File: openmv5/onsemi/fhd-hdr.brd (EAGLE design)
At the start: 35.6 x 16.5 mm, 75 parts, among them IC1 AR0231AT7C00XUEA0-DRBR-E, IC2 TLV62568PDDCR, IC3 MIC5365-2.8YC5-TR, J1 DF12-36-DP, Q1 PMXB120EPEZ

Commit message: Finish out new onsemi cameras
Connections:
- net SPI_MISO: now also IC1.K11
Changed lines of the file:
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@@
 <signal name="SPI_MISO" class="4">
 <contactref element="J1" pad="15"/>
+<contactref element="IC1" pad="K11"/>
+<wire x1="21.18" y1="4.89" x2="18.53" y2="10.8999" width="0" layer="19" extent="1-16"/>
 </signal>
 <signal name="SPI_MOSI" class="4">

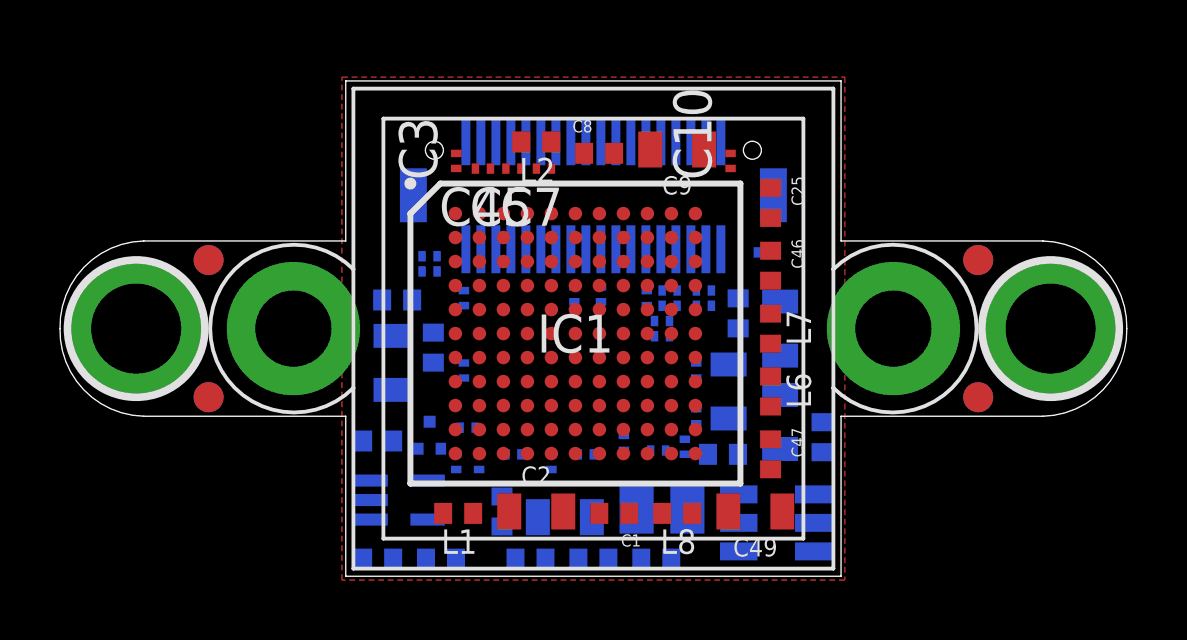
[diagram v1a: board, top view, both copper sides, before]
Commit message: Update camera modules to use different non-flippable pmosfet
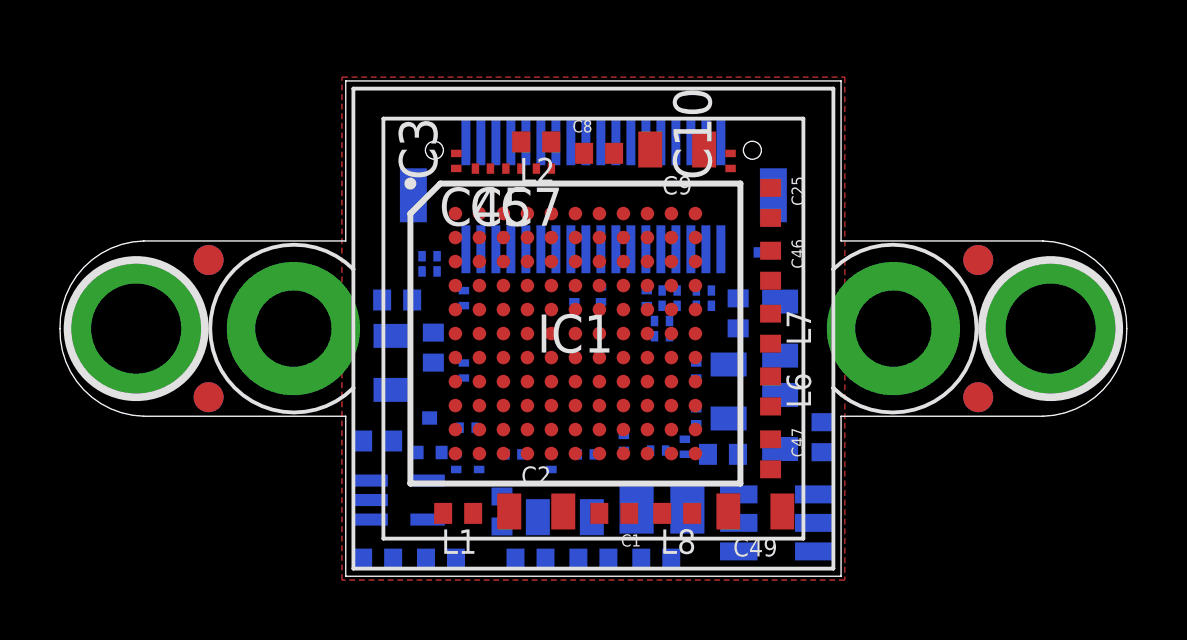
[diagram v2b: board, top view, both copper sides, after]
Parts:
- Q1: value PMXB120EPEZ -> SSM3J15FV,L3F; device PMXB120EPEZ:PMXB120EPEZ -> SSM3J15FV_L3F:SSM3J15FVL3F
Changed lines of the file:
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@@
 <attribute name="VALUE" x="15.875" y="1.27" size="0.6096" layer="27" font="vector" ratio="20" align="top-center"/>
 </element>
-<element name="Q1" library="PMXB120EPEZ" package="PMXB120EPEZ" value="PMXB120EPEZ" x="12.319" y="4.699" smashed="yes" rot="MR0">
-<attribute name="DESCRIPTION" value="MOSFET 30 V, P-channel Trench MOSFET" x="15.367" y="4.699" size="1.778" layer="28" rot="MR0" display="off"/>
-<attribute name="HEIGHT" value="0.4mm" x="15.367" y="4.699" size="1.778" layer="28" rot="MR0" display="off"/>
-<attribute name="MANUFACTURER_NAME" value="Nexperia" x="15.367" y="4.699" size="1.778" layer="28" rot="MR0" display="off"/>
-<attribute name="MANUFACTURER_PART_NUMBER" value="PMXB120EPEZ" x="15.367" y="4.699" size="1.778" layer="28" rot="MR0" display="off"/>
-<attribute name="MOUSER_PART_NUMBER" value="771-PMXB120EPEZ" x="15.367" y="4.699" size="1.778" layer="28" rot="MR0" display="off"/>
-<attribute name="MOUSER_PRICE-STOCK" value="https://www.mouser.co.uk/ProductDetail/Nexperia/PMXB120EPEZ?qs=gNSudQoqUYCYLaOobF3dPA%3D%3D" x="15.367" y="4.699" size="1.778" layer="28" rot="MR0" display="off"/>
-<attribute name="MPN" value="PMXB120EPEZ" x="15.367" y="4.699" size="1.778" layer="28" rot="MR0" display="off"/>
+<element name="Q1" library="SSM3J15FV_L3F" package="SSM3J15FVL3F" value="SSM3J15FV,L3F" x="12.319" y="4.699" smashed="yes" rot="MR0">
+<attribute name="DESCRIPTION" value="MOSFET Small-signal MOSFET High Speed Switching" x="15.367" y="4.699" size="1.778" layer="28" rot="MR0" display="off"/>
+<attribute name="HEIGHT" value="0.55mm" x="15.367" y="4.699" size="1.778" layer="28" rot="MR0" display="off"/>
+<attribute name="MANUFACTURER_NAME" value="Toshiba" x="15.367" y="4.699" size="1.778" layer="28" rot="MR0" display="off"/>
+<attribute name="MANUFACTURER_PART_NUMBER" value="SSM3J15FV,L3F" x="15.367" y="4.699" size="1.778" layer="28" rot="MR0" display="off"/>
+<attribute name="MOUSER_PART_NUMBER" value="757-SSM3J15FVL3F" x="15.367" y="4.699" size="1.778" layer="28" rot="MR0" display="off"/>
+<attribute name="MOUSER_PRICE-STOCK" value="https://www.mouser.co.uk/ProductDetail/Toshiba/SSM3J15FVL3F?qs=PDgMCp4xDJb4qTgE7FAUzA%3D%3D" x="15.367" y="4.699" size="1.778" layer="28" rot="MR0" display="off"/>
+<attribute name="MPN" value="SSM3J15FV,L3F" x="15.367" y="4.699" size="1.778" layer="28" rot="MR0" display="off"/>
 <attribute name="NAME" x="12.319" y="4.699" size="1.27" layer="26" rot="MR0" align="center"/>
 <attribute name="VALUE" x="12.319" y="4.699" size="1.27" layer="28" rot="MR0" align="center"/>
@@
 <contactref element="C31" pad="2"/>
 <contactref element="Q1" pad="2"/>
-<wire x1="10.1045" y1="0.5715" x2="10.353" y2="1.89" width="0" layer="19" extent="1-16"/>
-<wire x1="11.944" y1="4.249" x2="10.353" y2="1.89" width="0" layer="19" extent="16-16"/>
-<wire x1="21.53" y1="14.5001" x2="11.944" y2="4.249" width="0" layer="19" extent="16-16"/>
+<wire x1="11.919" y1="4.124" x2="21.53" y2="14.5001" width="0" layer="19" extent="16-16"/>
+<wire x1="10.353" y1="1.89" x2="11.919" y2="4.124" width="0" layer="19" extent="16-16"/>
+<wire x1="10.1045" y1="0.5715" x2="10.353" y2="1.89" width="0" layer="19" extent="16-16"/>
 </signal>
 <signal name="VCC" class="3">
@@
 <contactref element="J1" pad="25"/>
 <contactref element="Q1" pad="1"/>
-<wire x1="16.03" y1="10.8999" x2="12.694" y2="4.249" width="0" layer="19" extent="1-16"/>
+<wire x1="12.719" y1="4.124" x2="16.03" y2="10.8999" width="0" layer="19" extent="16-16"/>
 </signal>
 <signal name="DCMI_D4" class="4">
@@
 <contactref element="R4" pad="1"/>
 <contactref element="Q1" pad="3"/>
-<wire x1="11.1045" y1="4.5085" x2="10.353" y2="3.19" width="0" layer="19" extent="16-16"/>
-<wire x1="12.319" y1="5.149" x2="11.1045" y2="4.5085" width="0" layer="19" extent="16-16"/>
+<wire x1="11.1045" y1="4.5085" x2="12.319" y2="5.274" width="0" layer="19" extent="16-16"/>
+<wire x1="10.353" y1="3.19" x2="11.1045" y2="4.5085" width="0" layer="19" extent="16-16"/>
 </signal>
 <signal name="RESET_N" class="4">
